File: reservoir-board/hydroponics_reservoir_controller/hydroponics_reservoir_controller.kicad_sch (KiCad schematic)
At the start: 82 parts, among them J1 Jumper, J2 Conn_01x04_Socket, J5 i2c_Peripherals, J6 1Wire_Peripherals, Q1 AO3400A, Q2 AO3400A, Q3 AO3400A, Q4 AO3400A, Q5 AO3400A, Q6 AO3400A, Q7 AO3400A, Q8 AO3400A, U1 ESP32, U2 SP3485EN, U3 AMS1117-3.3, U4 TPS54302

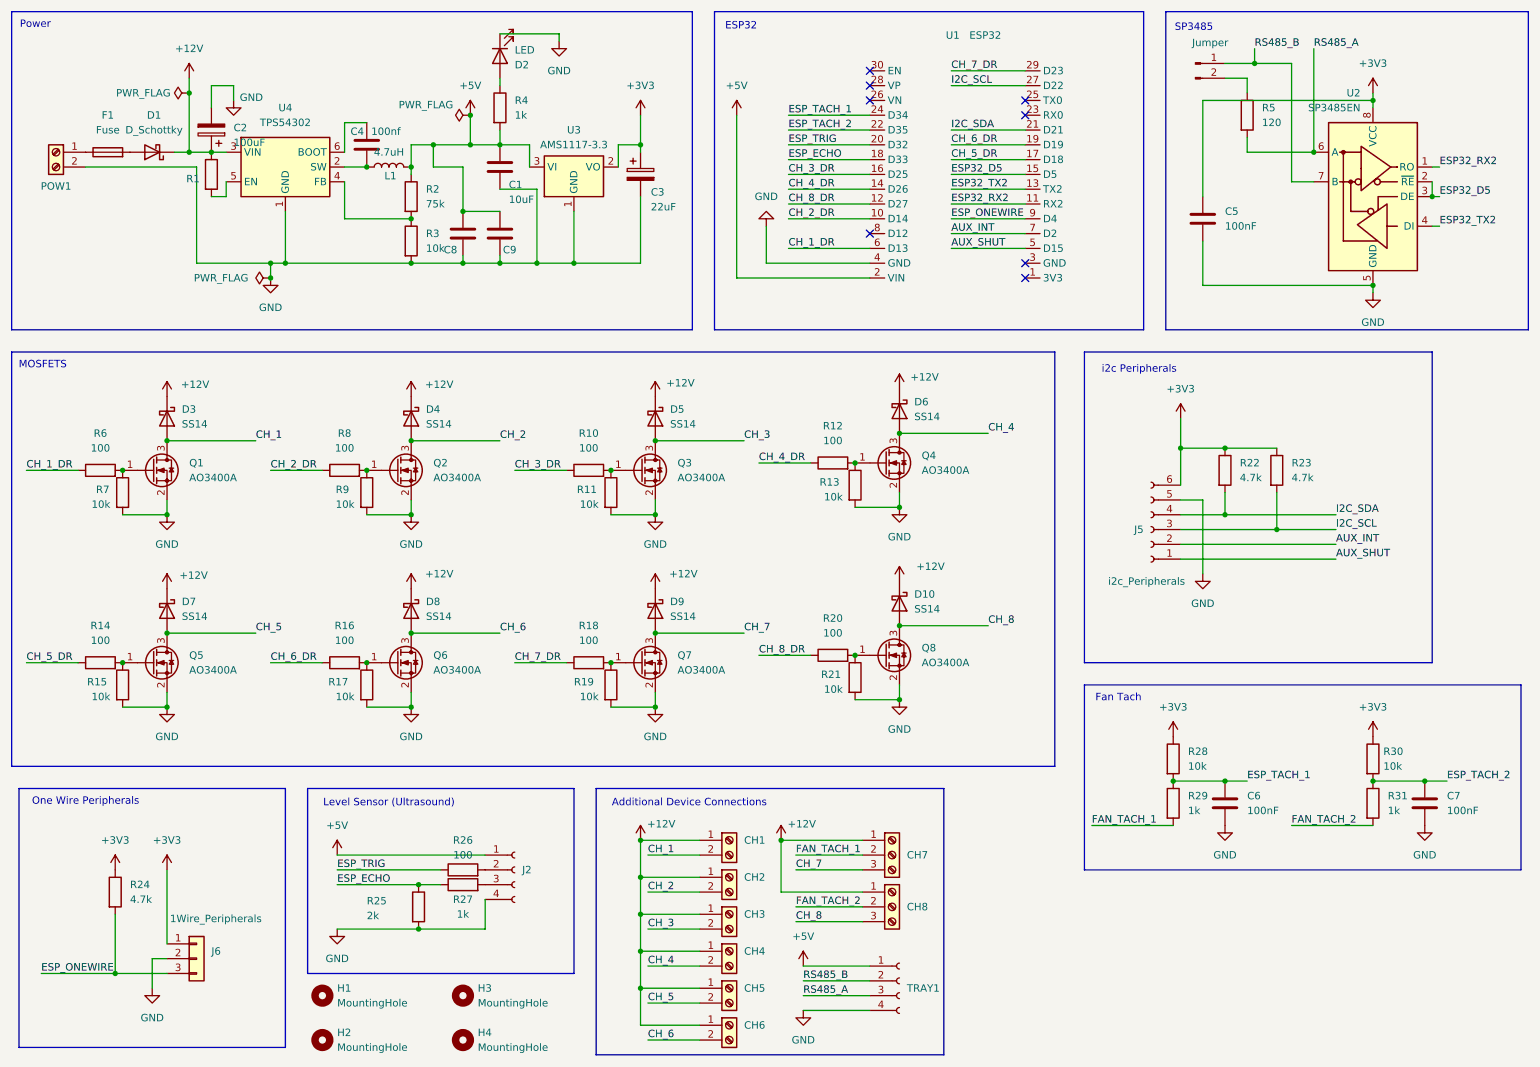
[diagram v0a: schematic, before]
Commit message: JLCPCB prep: fab.sh cleanup, DNP the ESP32 module, BOM part-value fixes
tools/fab.sh:
- Gerbers use Protel extensions (JLCPCB's preferred naming) instead of
  --no-protel-ext.
- Drill export splits PTH/NPTH into separate Excellon files
  (--excellon-separate-th) instead of one merged file.
- BOM export now pulls the LCSC field (matching what's actually used in
  the schematics) instead of a nonexistent MPN field, groups by
  Value+Footprint+LCSC so parts sharing a value but not an LCSC code
  don't get merged together and silently lose their code, and excludes
  DNP parts.
- Pick-and-place (now named *-cpl.csv) already excluded DNP/THT; BOM
  now matches.
- Final zip only includes the gerbers + drill files JLCPCB needs, not
  the .gbrjob/drill-map files kicad-cli also generates.
- ERC gate relaxed to error-only: a stale lib_symbol_mismatch warning
  on the ESP32 symbol (harmless - doesn't affect connectivity or fab
  output) was blocking the pipeline; DRC stays error+warning.

Mark the socketed ESP32 DevKit (U1) Do-Not-Populate in both boards'
schematics, since it's a module the user fits themselves rather than
something JLCPCB should source/place - this drops it from BOM and CPL
automatically.

Fix a stale pin-number mismatch in reservoir-board's New_Library.kicad_sym
(ESP32 EN pin was "" in the library file but "30" in the schematic's
cached copy) that was one cause of the ERC warning above.

Also includes reservoir-board BOM part-value corrections (D_Schottky ->
SS34, bare resistor values -> "<value> Ohm") made directly in KiCad.

Co-Authored-By: Claude Sonnet 5 <noreply@anthropic.com>
Claude-Session: https://claude.ai/code/session_01QYbZEgBzGJ6rSai1ie8nG1
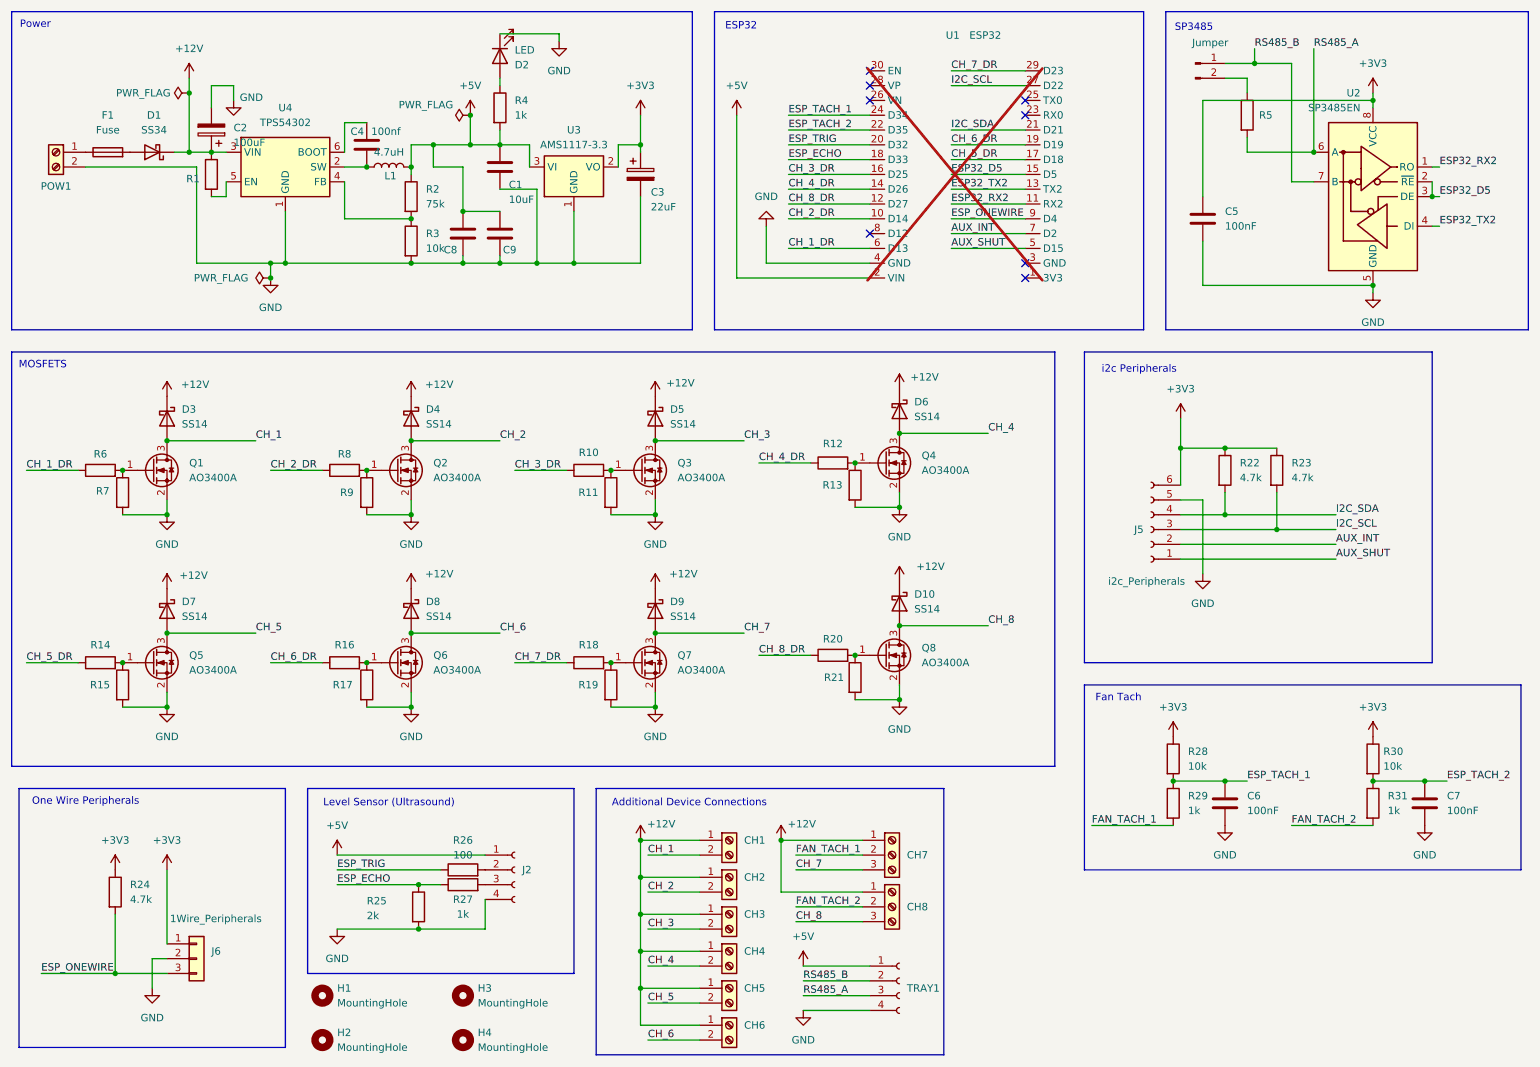
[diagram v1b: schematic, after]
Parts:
- D1: value D_Schottky -> SS34; LCSC (none) -> C8678
- D3: LCSC (none) -> C1508
- R10, R12, R14, R16, R18, R20, R6, R8: value 100 -> 100 Ohm
- R5: value 120 -> 120 Ohm
- U1: now not fitted
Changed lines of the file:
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@@
 		(in_pos_files yes)
 		(dnp no)
-		(fields_autoplaced yes)
 		(property "Reference" "R10"
-			(at 113.03 88.9 90)
+			(at 113.03 92.202 90)
 			(show_name no)
 			(do_not_autoplace no)
@@
 			)
 		)
-		(property "Value" "100"
+		(property "Value" "100 Ohm"
 			(at 113.03 91.44 90)
+			(hide yes)
 			(show_name no)
 			(do_not_autoplace no)
@@
 		(in_pos_files yes)
 		(dnp no)
-		(fields_autoplaced yes)
 		(property "Reference" "R18"
-			(at 113.03 121.92 90)
+			(at 113.03 125.222 90)
 			(show_name no)
 			(do_not_autoplace no)
@@
 			)
 		)
-		(property "Value" "100"
+		(property "Value" "100 Ohm"
 			(at 113.03 124.46 90)
+			(hide yes)
 			(show_name no)
 			(do_not_autoplace no)
@@
 		(in_pos_files yes)
 		(dnp no)
-		(fields_autoplaced yes)
 		(property "Reference" "R8"
-			(at 71.12 88.9 90)
+			(at 71.12 92.456 90)
 			(show_name no)
 			(do_not_autoplace no)
@@
 			)
 		)
-		(property "Value" "100"
+		(property "Value" "100 Ohm"
 			(at 71.12 91.44 90)
+			(hide yes)
 			(show_name no)
 			(do_not_autoplace no)
@@
 		(dnp no)
 		(property "Reference" "R11"
-			(at 110.998 98.552 0)
+			(at 111.252 99.06 0)
 			(show_name no)
 			(do_not_autoplace no)
@@
 		(property "Value" "10k"
 			(at 111.506 101.092 0)
+			(hide yes)
 			(show_name no)
 			(do_not_autoplace no)
@@
 		(dnp no)
 		(property "Reference" "R19"
-			(at 110.49 131.572 0)
+			(at 111.252 132.08 0)
 			(show_name no)
 			(do_not_autoplace no)
@@
 		(property "Value" "10k"
 			(at 111.506 134.112 0)
+			(hide yes)
 			(show_name no)
 			(do_not_autoplace no)
@@
 		(dnp no)
 		(property "Reference" "R7"
-			(at 28.448 98.552 0)
+			(at 28.448 98.806 0)
 			(show_name no)
 			(do_not_autoplace no)
@@
 		(property "Value" "10k"
 			(at 27.686 101.092 0)
+			(hide yes)
 			(show_name no)
 			(do_not_autoplace no)
@@
 		(in_pos_files yes)
 		(dnp no)
-		(fields_autoplaced yes)
 		(property "Reference" "R5"
-			(at 228.6 33.0199 0)
+			(at 228.092 34.29 0)
 			(show_name no)
 			(do_not_autoplace no)
@@
 			)
 		)
-		(property "Value" "120"
+		(property "Value" "120 Ohm"
 			(at 228.6 35.5599 0)
+			(hide yes)
 			(show_name no)
 			(do_not_autoplace no)
@@
 		(dnp no)
 		(property "Reference" "R21"
-			(at 152.908 130.302 0)
+			(at 153.416 130.81 0)
 			(show_name no)
 			(do_not_autoplace no)
@@
 		(property "Value" "10k"
 			(at 153.416 132.842 0)
+			(hide yes)
 			(show_name no)
 			(do_not_autoplace no)
@@
 		(dnp no)
 		(property "Reference" "R17"
-			(at 68.326 131.572 0)
+			(at 69.088 132.08 0)
 			(show_name no)
 			(do_not_autoplace no)
@@
 		(property "Value" "10k"
 			(at 69.596 134.112 0)
+			(hide yes)
 			(show_name no)
 			(do_not_autoplace no)
@@
 		(in_pos_files yes)
 		(dnp no)
-		(fields_autoplaced yes)
 		(property "Reference" "R6"
-			(at 29.21 88.9 90)
+			(at 29.21 92.456 90)
 			(show_name no)
 			(do_not_autoplace no)
@@
 			)
 		)
-		(property "Value" "100"
+		(property "Value" "100 Ohm"
 			(at 29.21 91.44 90)
+			(hide yes)
 			(show_name no)
 			(do_not_autoplace no)
@@
 		(dnp no)
 		(property "Reference" "R13"
-			(at 152.654 97.282 0)
+			(at 153.162 97.79 0)
 			(show_name no)
 			(do_not_autoplace no)
@@
 		(property "Value" "10k"
 			(at 153.416 99.822 0)
+			(hide yes)
 			(show_name no)
 			(do_not_autoplace no)
@@
 		(in_pos_files yes)
 		(dnp no)
-		(fields_autoplaced yes)
 		(property "Reference" "R20"
-			(at 154.94 120.65 90)
+			(at 154.94 124.206 90)
 			(show_name no)
 			(do_not_autoplace no)
@@
 			)
 		)
-		(property "Value" "100"
+		(property "Value" "100 Ohm"
 			(at 154.94 123.19 90)
+			(hide yes)
 			(show_name no)
 			(do_not_autoplace no)
@@
 		(in_pos_files yes)
 		(dnp no)
-		(fields_autoplaced yes)
 		(property "Reference" "R12"
-			(at 154.94 87.63 90)
+			(at 154.94 90.678 90)
 			(show_name no)
 			(do_not_autoplace no)
@@
 			)
 		)
-		(property "Value" "100"
+		(property "Value" "100 Ohm"
 			(at 154.94 90.17 90)
+			(hide yes)
 			(show_name no)
 			(do_not_autoplace no)
@@
 		(dnp no)
 		(property "Reference" "R15"
-			(at 26.924 131.572 0)
+			(at 27.432 132.08 0)
 			(show_name no)
 			(do_not_autoplace no)
@@
 		(property "Value" "10k"
 			(at 27.686 134.112 0)
+			(hide yes)
 			(show_name no)
 			(do_not_autoplace no)
@@
 		(dnp no)
 		(property "Reference" "R9"
-			(at 69.596 98.552 0)
+			(at 70.358 99.06 0)
 			(show_name no)
 			(do_not_autoplace no)
@@
 		(property "Value" "10k"
 			(at 69.596 101.092 0)
+			(hide yes)
 			(show_name no)
 			(do_not_autoplace no)
@@
 		(in_pos_files yes)
 		(dnp no)
-		(fields_autoplaced yes)
 		(property "Reference" "R14"
-			(at 29.21 121.92 90)
+			(at 29.21 125.222 90)
 			(show_name no)
 			(do_not_autoplace no)
@@
 			)
 		)
-		(property "Value" "100"
+		(property "Value" "100 Ohm"
 			(at 29.21 124.46 90)
+			(hide yes)
 			(show_name no)
 			(do_not_autoplace no)
@@
 			)
 		)
-		(property "Value" "D_Schottky"
+		(property "Value" "SS34"
 			(at 38.4175 36.83 0)
 			(show_name no)
@@
 			)
 		)
+		(property "LCSC" "C8678"
+			(at 38.1 40.64 0)
+			(hide yes)
+			(show_name no)
+			(do_not_autoplace no)
+			(effects
+				(font
+					(size 1.27 1.27)
+				)
+			)
+		)
 		(pin "1"
 		)
@@
 		(in_pos_files yes)
 		(dnp no)
-		(fields_autoplaced yes)
 		(property "Reference" "R16"
-			(at 71.12 121.92 90)
+			(at 71.12 125.222 90)
 			(show_name no)
 			(do_not_autoplace no)
@@
 			)
 		)
-		(property "Value" "100"
+		(property "Value" "100 Ohm"
 			(at 71.12 124.46 90)
+			(hide yes)
 			(show_name no)
 			(do_not_autoplace no)
@@
 		(on_board yes)
 		(in_pos_files yes)
-		(dnp no)
+		(dnp yes)
 		(property "Reference" "U1"
 			(at 175.514 20.574 0)
@@
 			(hide yes)
 			(show_name no)
+			(do_not_autoplace no)
+			(effects
+				(font
+					(size 1.27 1.27)
+				)
+			)
+		)
+		(property "LCSC" "C1508"
+			(at 40.64 86.36 90)
+			(hide yes)
+			(show_name no)

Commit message: reservoir-board: populate LCSC part numbers for the full BOM
Added an LCSC property to every BOM line that was missing one (75
component references across resistors, capacitors, connectors,
terminal blocks, MOSFETs, ICs, the inductor, and the fuse), researched
and cross-checked against LCSC's own product listings rather than
assumed. D1/D3 already had codes from earlier manual work; applied
D3's SS14 code to the other seven SS14 diodes (D4-D10) so they merge
into one BOM line instead of sitting uncoded.

F1 (resettable fuse) is C207091 (Littelfuse 2920L500/16MR) - 2920
package matches the existing footprint, 5A hold current, 16V rather
than the originally-wanted 30V (accepted knowingly; LCSC doesn't stock
a 5A part rated higher in this package).

Capacitor voltage ratings were not specified anywhere in the schematic,
so picked per rail context (>=25V for parts likely on the +12V input,
>=16V for +5V/3.3V) - flagged for review rather than assumed silently.

Freshly-exported BOM confirmed clean: every non-DNP line now has an
LCSC Part #, correctly grouped (e.g. R26 merges into the 9-part 100 Ohm
group, D3-D10 merge into one 8-part SS14 line).

Co-Authored-By: Claude Sonnet 5 <noreply@anthropic.com>
Claude-Session: https://claude.ai/code/session_01QYbZEgBzGJ6rSai1ie8nG1
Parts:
- C1: LCSC (none) -> C2443257
- C2: LCSC (none) -> C970685
- C3: LCSC (none) -> C24518
- C4: LCSC (none) -> C93194
- C5, C6, C7: LCSC (none) -> C83055
- C8, C9: LCSC (none) -> C105213
- CH1, CH2, CH3, CH4, CH5, CH6: LCSC (none) -> C474892
- CH7, CH8: LCSC (none) -> C474893
- D10, D4, D5, D6, D7, D8, D9: LCSC (none) -> C1508
- D2: LCSC (none) -> C84260
- F1: LCSC (none) -> C207091
- J1: LCSC (none) -> C36717
- J2, TRAY1: LCSC (none) -> C144395
- J5: LCSC (none) -> C144397
- J6: LCSC (none) -> C144394
- L1: LCSC (none) -> C2047389
- POW1: LCSC (none) -> C474881
- Q1, Q2, Q3, Q4, Q5, Q6, Q7, Q8: LCSC (none) -> C20917
- R1: LCSC (none) -> C17407
- R10, R12, R14, R16, R18, R20, R6, R8: LCSC (none) -> C17408
- R11, R13, R15, R17, R19, R21, R28, R3, R30, R7, R9: LCSC (none) -> C17414
- R2: LCSC (none) -> C17819
- R22, R23, R24: LCSC (none) -> C17673
- R25: LCSC (none) -> C17604
- R26: value 100 -> 100 Ohm; LCSC (none) -> C17408
- R27, R29, R31, R4: LCSC (none) -> C17513
- R5: LCSC (none) -> C17437
- U2: LCSC (none) -> C8963
- U3: LCSC (none) -> C6186
- U4: LCSC (none) -> C311983

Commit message: reservoir-board: fix 4 out-of-stock/invalid LCSC codes; add stock checker
JLCPCB rejected the order over parts shortages (C8/C9, L1, R1) and
"D3-D10 don't have parts defined." Checked each directly against LCSC:

- C1508 (D3-D10, SS14) doesn't exist on LCSC at all - it 404s, or on a
  retry silently redirects to an unrelated part (C293349). This was
  the user's own prior manual-workflow data, never actually valid.
  Replaced with C466498 (High Diode SS14, SMA, verified in stock).
- C105213 (C8,C9, 22uF 1206 X5R) and C2047389 (L1, Bourns
  SRP6060FA-4R7M) are both genuinely 0 stock on LCSC. Replaced with
  C338055 (TDK, same 22uF/25V/X5R/1206 spec) and C2046759 (Bourns
  SRP6060FA-100M, 10uH - same footprint/family, guaranteed to fit the
  existing pads; value bumped from 4.7uH since no in-stock part at the
  original value had a confirmed-matching footprint).
- C17407 (R1, 100k 0805 1%) shows 188k in stock on LCSC's general
  marketplace, so this one is likely a JLCPCB assembly-line-specific
  pool constraint the general stock number doesn't reflect - not
  something tools/check_stock.py can catch. Swapped to a different
  manufacturer anyway (C96346, Yageo, same spec) to sidestep it.

Added tools/check_stock.py: LCSC embeds live stock numbers as
server-rendered JSON on its product pages, so a plain HTTP GET with a
browser User-Agent is enough to check every LCSC code in a BOM - no
API key needed. Also catches invalid/delisted codes by checking the
page's own productCode against what was requested (a bad code doesn't
always 404 - it can silently redirect to an unrelated part, which is
exactly what happened with C1508). Wired into fab.sh right after the
BOM is finalized, gating the same way ERC/DRC do. Known limitation:
checks LCSC's general marketplace stock, not JLCPCB's own assembly
pool - R1 above is a live example of that gap.

Co-Authored-By: Claude Sonnet 5 <noreply@anthropic.com>
Claude-Session: https://claude.ai/code/session_01QYbZEgBzGJ6rSai1ie8nG1
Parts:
- C8, C9: LCSC C105213 -> C338055
- D10, D3, D4, D5, D6, D7, D8, D9: LCSC C1508 -> C466498
- L1: value 4.7uH -> 10uH; LCSC C2047389 -> C2046759
- R1: LCSC C17407 -> C96346
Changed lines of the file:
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@@
 			)
 		)
-					(property "LCSC" "C17407"
+					(property "LCSC" "C96346"
 				(at 48.26 44.45 0)
 				(hide yes)
@@
 			)
 		)
-					(property "LCSC" "C105213"
+					(property "LCSC" "C338055"
 				(at 91.44 54.61 0)
 				(hide yes)
@@
 			)
 		)
-		(property "Value" "4.7uH"
+		(property "Value" "10uH"
 			(at 78.74 40.64 90)
 			(show_name no)
@@
 			)
 		)
-					(property "LCSC" "C2047389"
+					(property "LCSC" "C2046759"
 				(at 78.74 43.18 0)
 				(hide yes)
@@
 			)
 		)
-					(property "LCSC" "C1508"
+					(property "LCSC" "C466498"
 				(at 166.37 85.09 0)
 				(hide yes)
@@
 			)
 		)
-					(property "LCSC" "C1508"
+					(property "LCSC" "C466498"
 				(at 124.46 119.38 0)
 				(hide yes)
@@
 			)
 		)
-					(property "LCSC" "C1508"
+					(property "LCSC" "C466498"
 				(at 166.37 118.11 0)
 				(hide yes)
@@
 			)
 		)
-					(property "LCSC" "C1508"
+					(property "LCSC" "C466498"
 				(at 124.46 86.36 0)
 				(hide yes)
@@
 			)
 		)
-					(property "LCSC" "C1508"
+					(property "LCSC" "C466498"
 				(at 82.55 119.38 0)
 				(hide yes)
@@
 			)
 		)
-					(property "LCSC" "C1508"
+					(property "LCSC" "C466498"
 				(at 40.64 119.38 0)
 				(hide yes)
@@
 			)
 		)
-					(property "LCSC" "C105213"
+					(property "LCSC" "C338055"
 				(at 97.79 54.61 0)
 				(hide yes)
@@
 			)
 		)
-		(property "LCSC" "C1508"
+		(property "LCSC" "C466498"
 			(at 40.64 86.36 90)
 			(hide yes)
@@
 			)
 		)
-					(property "LCSC" "C1508"
+					(property "LCSC" "C466498"
 				(at 82.55 86.36 0)
 				(hide yes)
